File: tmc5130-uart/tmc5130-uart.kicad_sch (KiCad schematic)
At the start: 0 parts

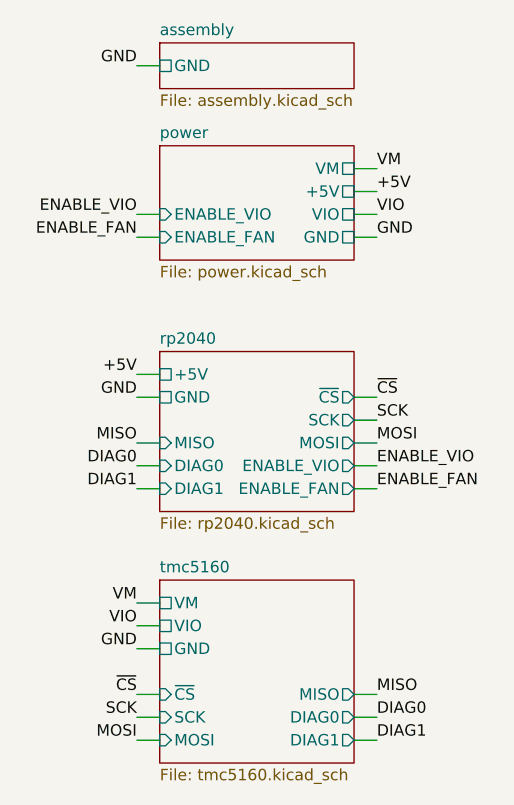
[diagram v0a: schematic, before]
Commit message: Delete unused schematics
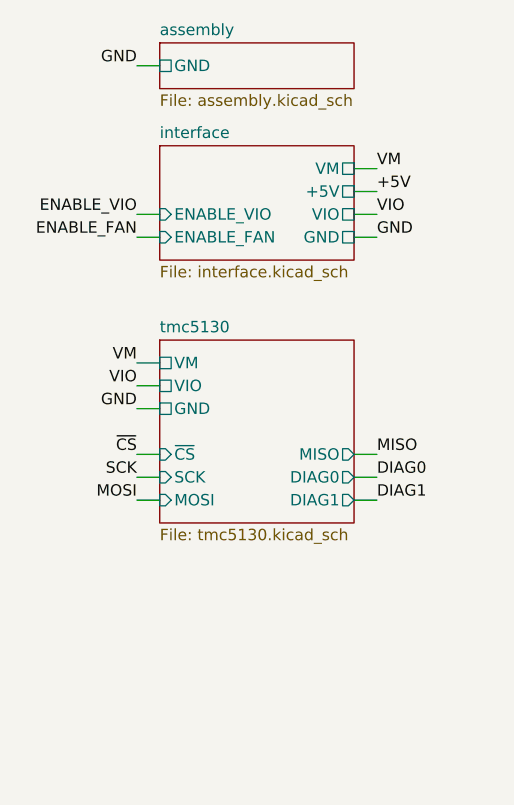
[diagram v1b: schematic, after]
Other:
- sheet power renamed interface
- sheet tmc5160 renamed tmc5130
- removed sheet rp2040
- sheet interface: file power.kicad_sch -> interface.kicad_sch
- sheet tmc5130: file tmc5160.kicad_sch -> tmc5130.kicad_sch

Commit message: Add components from jlcpcb
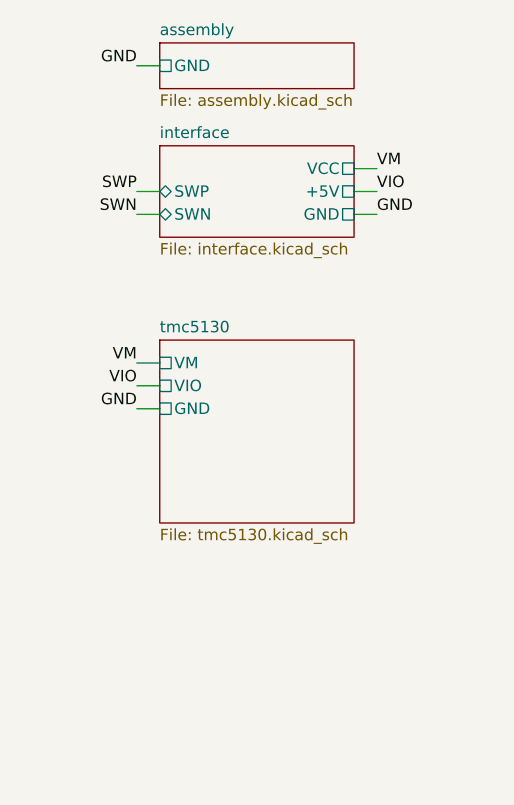
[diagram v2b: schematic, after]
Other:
- sheet interface ports: added SWN, SWP, VCC; removed ENABLE_FAN, ENABLE_VIO, VIO, VM
- sheet tmc5130 ports: added none; removed DIAG0, DIAG1, MISO, MOSI, SCK, ~{CS}
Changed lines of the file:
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@@
   (title_block
     (title "tmc5130-uart")
-    (date "2024-06-27")
+    (date "2024-07-02")
     (rev "1.0")
     (company "Howard Hughes Medical Institute")
   )
-  (wire (pts (xy 130.81 101.6) (xy 128.27 101.6))
-    (stroke (width 0) (type default))
-  )
-  (wire (pts (xy 130.81 74.93) (xy 128.27 74.93))
-    (stroke (width 0) (type default))
-  )
-  (wire (pts (xy 154.94 69.85) (xy 152.4 69.85))
+  (wire (pts (xy 130.81 72.39) (xy 128.27 72.39))
     (stroke (width 0) (type default))
   )
@@
     (stroke (width 0) (type default))
   )
-  (wire (pts (xy 130.81 104.14) (xy 128.27 104.14))
-    (stroke (width 0) (type default))
-  )
   (wire (pts (xy 154.94 67.31) (xy 152.4 67.31))
-    (stroke (width 0) (type default))
-  )
-  (wire (pts (xy 130.81 99.06) (xy 128.27 99.06))
-    (stroke (width 0) (type default))
-  )
-  (wire (pts (xy 152.4 104.14) (xy 154.94 104.14))
     (stroke (width 0) (type default))
   )
@@
     (stroke (width 0) (type default))
   )
-  (wire (pts (xy 152.4 101.6) (xy 154.94 101.6))
-    (stroke (width 0) (type default))
-  )
-  (wire (pts (xy 152.4 99.06) (xy 154.94 99.06))
-    (stroke (width 0) (type default))
-  )
   (wire (pts (xy 128.27 93.98) (xy 130.81 93.98))
-    (stroke (width 0) (type default))
-  )
-  (wire (pts (xy 154.94 74.93) (xy 152.4 74.93))
     (stroke (width 0) (type default))
   )
@@
     (stroke (width 0) (type default))
   )
-  (wire (pts (xy 130.81 72.39) (xy 128.27 72.39))
+  (wire (pts (xy 154.94 69.85) (xy 152.4 69.85))
     (stroke (width 0) (type default))
   )
-  (label "GND" (at 154.94 74.93 0) (fields_autoplaced)
+  (wire (pts (xy 130.81 69.85) (xy 128.27 69.85))
+    (stroke (width 0) (type default))
+  )
+  (label "GND" (at 154.94 72.39 0) (fields_autoplaced)
     (effects (font (size 1.27 1.27)) (justify left bottom))
   )
-  (label "DIAG1" (at 154.94 104.14 0) (fields_autoplaced)
+  (label "VIO" (at 154.94 69.85 0) (fields_autoplaced)
     (effects (font (size 1.27 1.27)) (justify left bottom))
-  )
-  (label "VIO" (at 154.94 72.39 0) (fields_autoplaced)
-    (effects (font (size 1.27 1.27)) (justify left bottom))
-  )
-  (label "+5V" (at 154.94 69.85 0) (fields_autoplaced)
-    (effects (font (size 1.27 1.27)) (justify left bottom))
-  )
-  (label "MOSI" (at 128.27 104.14 180) (fields_autoplaced)
-    (effects (font (size 1.27 1.27)) (justify right bottom))
   )
   (label "VIO" (at 128.27 91.44 180) (fields_autoplaced)
@@
     (effects (font (size 1.27 1.27)) (justify right bottom))
   )
-  (label "DIAG0" (at 154.94 101.6 0) (fields_autoplaced)
-    (effects (font (size 1.27 1.27)) (justify left bottom))
-  )
   (label "GND" (at 128.27 55.88 180) (fields_autoplaced)
     (effects (font (size 1.27 1.27)) (justify right bottom))
@@
     (effects (font (size 1.27 1.27)) (justify right bottom))
   )
-  (label "MISO" (at 154.94 99.06 0) (fields_autoplaced)
-    (effects (font (size 1.27 1.27)) (justify left bottom))
-  )
-  (label "ENABLE_VIO" (at 128.27 72.39 180) (fields_autoplaced)
+  (label "SWP" (at 128.27 69.85 180) (fields_autoplaced)
     (effects (font (size 1.27 1.27)) (justify right bottom))
   )
-  (label "SCK" (at 128.27 101.6 180) (fields_autoplaced)
-    (effects (font (size 1.27 1.27)) (justify right bottom))
-  )
-  (label "~{CS}" (at 128.27 99.06 180) (fields_autoplaced)
-    (effects (font (size 1.27 1.27)) (justify right bottom))
-  )
-  (label "ENABLE_FAN" (at 128.27 74.93 180) (fields_autoplaced)
+  (label "SWN" (at 128.27 72.39 180) (fields_autoplaced)
     (effects (font (size 1.27 1.27)) (justify right bottom))
   )
@@
     )
     (pin "GND" passive (at 130.81 93.98 180)
-      (effects (font (size 1.27 1.27)) (justify left))
-    )
-    (pin "~{CS}" input (at 130.81 99.06 180)
-      (effects (font (size 1.27 1.27)) (justify left))
-    )
-    (pin "SCK" input (at 130.81 101.6 180)
-      (effects (font (size 1.27 1.27)) (justify left))
-    )
-    (pin "DIAG0" output (at 152.4 101.6 0)
-      (effects (font (size 1.27 1.27)) (justify right))
-    )
-    (pin "DIAG1" output (at 152.4 104.14 0)
-      (effects (font (size 1.27 1.27)) (justify right))
-    )
-    (pin "MISO" output (at 152.4 99.06 0)
-      (effects (font (size 1.27 1.27)) (justify right))
-    )
-    (pin "MOSI" input (at 130.81 104.14 180)
       (effects (font (size 1.27 1.27)) (justify left))
     )
@@
     )
   )
-  (sheet (at 130.81 64.77) (size 21.59 12.7) (fields_autoplaced)
+  (sheet (at 130.81 64.77) (size 21.59 10.16) (fields_autoplaced)
     (stroke (width 0.1524) (type solid))
     (fill (color 0 0 0 0.0000))
@@
       (effects (font (size 1.27 1.27)) (justify left bottom))
     )
-    (property "Sheetfile" "interface.kicad_sch" (at 130.81 78.0546 0)
+    (property "Sheetfile" "interface.kicad_sch" (at 130.81 75.5146 0)
       (effects (font (size 1.27 1.27)) (justify left top))
     )
-    (pin "GND" passive (at 152.4 74.93 0)
+    (pin "GND" passive (at 152.4 72.39 0)
       (effects (font (size 1.27 1.27)) (justify right))
-    )
-    (pin "VM" passive (at 152.4 67.31 0)
-      (effects (font (size 1.27 1.27)) (justify right))
-    )
-    (pin "VIO" passive (at 152.4 72.39 0)
-      (effects (font (size 1.27 1.27)) (justify right))
-    )
-    (pin "ENABLE_VIO" input (at 130.81 72.39 180)
-      (effects (font (size 1.27 1.27)) (justify left))
-    )
-    (pin "ENABLE_FAN" input (at 130.81 74.93 180)
-      (effects (font (size 1.27 1.27)) (justify left))
     )
     (pin "+5V" passive (at 152.4 69.85 0)
       (effects (font (size 1.27 1.27)) (justify right))
     )
+    (pin "SWN" bidirectional (at 130.81 72.39 180)
+      (effects (font (size 1.27 1.27)) (justify left))
+    )
+    (pin "SWP" bidirectional (at 130.81 69.85 180)
+      (effects (font (size 1.27 1.27)) (justify left))
+    )
+    (pin "VCC" passive (at 152.4 67.31 0)
+      (effects (font (size 1.27 1.27)) (justify right))
+    )

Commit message: Add components
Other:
- sheet interface ports: added VAA; removed VCC
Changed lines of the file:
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@@
   (title_block
     (title "tmc5130-uart")
-    (date "2024-07-02")
+    (date "2024-07-11")
     (rev "1.0")
     (company "Howard Hughes Medical Institute")
@@
       (effects (font (size 1.27 1.27)) (justify left))
     )
-    (pin "VCC" passive (at 152.4 67.31 0)
+    (pin "VAA" passive (at 152.4 67.31 0)
       (effects (font (size 1.27 1.27)) (justify right))
     )
